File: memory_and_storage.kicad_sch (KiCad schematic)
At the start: 5 parts, among them J3 503182-1852, U7 MR25H40MDF

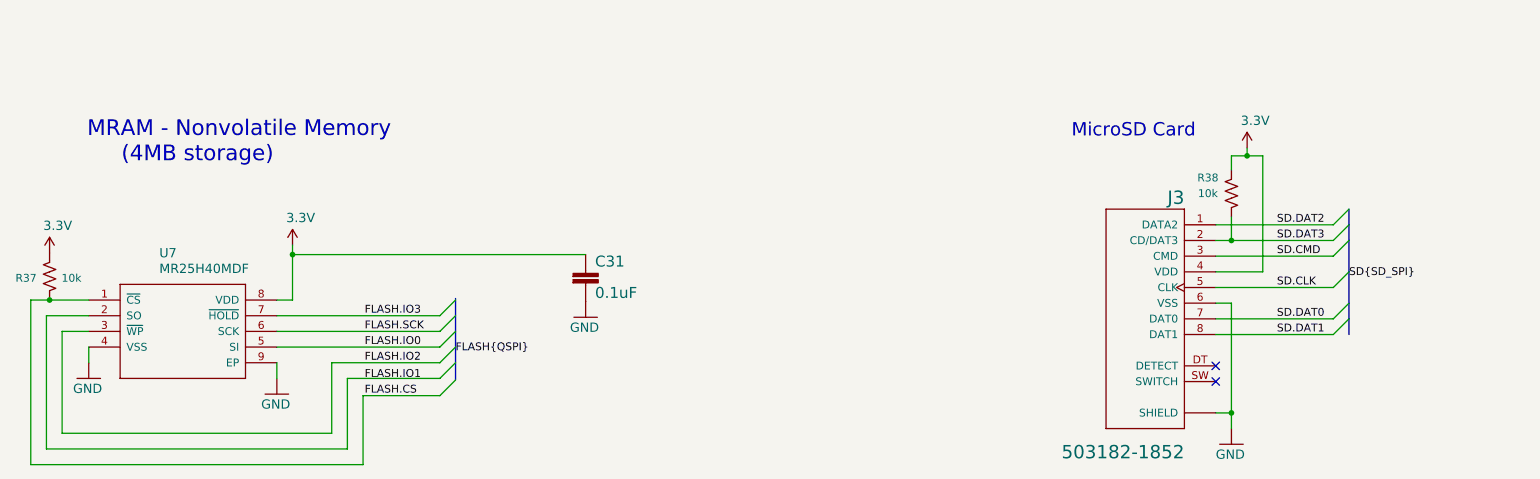
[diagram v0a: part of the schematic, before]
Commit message: schematic update
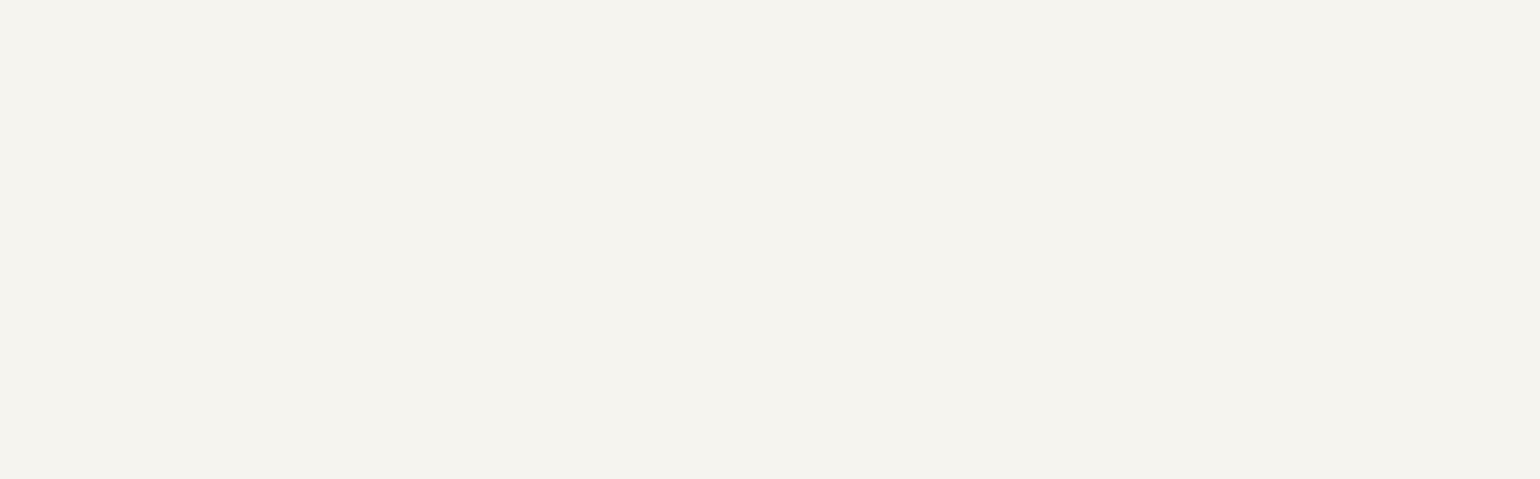
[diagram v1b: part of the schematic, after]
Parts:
- removed C31: 0.1uF, Capacitor_SMD:C_0603_1608Metric, symbol mainboard:2.2UF-0603-10V-20%
- removed J3: 503182-1852, mainboard:MOLEX_503182-1852, symbol mainboard:503182-1852
- removed R37, R38: 10k, Resistor_SMD:R_0603_1608Metric, symbol Device:R_US
- removed U7: MR25H40MDF, mainboard:SON127P600X500X90-9N, symbol mainboard:MR25H40MDF
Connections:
- no-connect marks 2 -> 0
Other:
- note removed: "MRAM - Nonvolatile Memory (4MB storage)"
- note removed: "MicroSD Card"
